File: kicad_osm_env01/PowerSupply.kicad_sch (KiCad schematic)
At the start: 28 parts, among them J5 USB_C_Receptacle_USB2.0, U1 LM66100DCKR, U4 LM66100DCKR, U9 TLV1117LV33DCYR

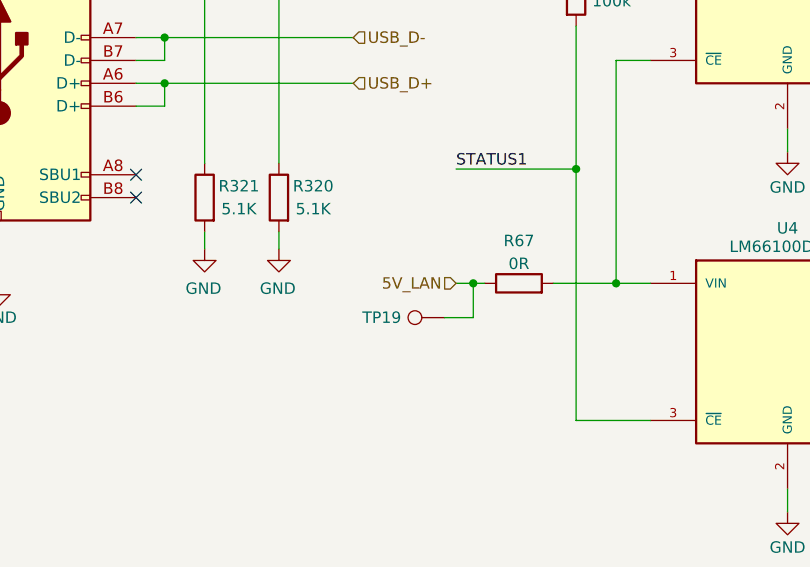
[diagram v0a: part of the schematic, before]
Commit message: locked in main connectors for connector end on layout
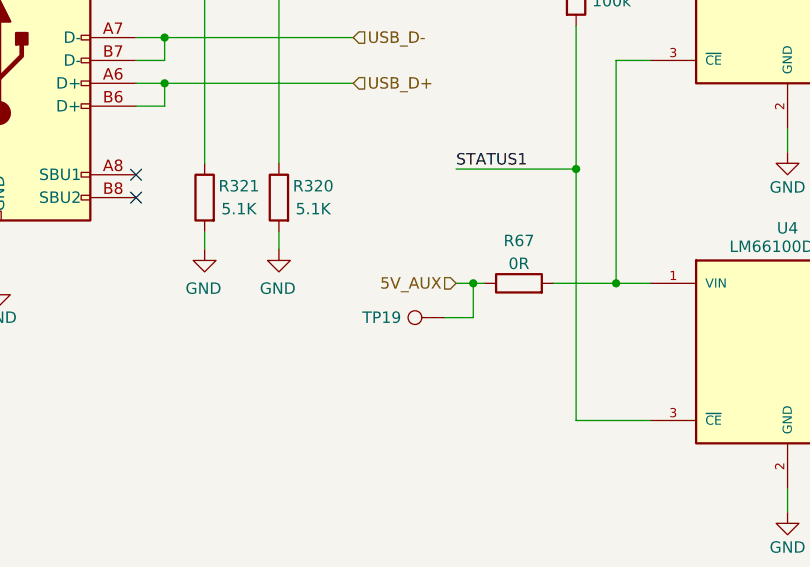
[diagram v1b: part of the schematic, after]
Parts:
- J5: footprint Footprints:MOLEX_216989-0001 -> Devtank_PCB_lib:216989-0001_MOL
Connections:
- net 5V_LAN renamed 5V_AUX
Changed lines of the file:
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@@
     (effects (font (size 1.27 1.27)) (justify left))
   )
-  (hierarchical_label "5V_LAN" (shape input) (at 81.28 75.565 180) (fields_autoplaced)
+  (hierarchical_label "5V_AUX" (shape input) (at 81.28 75.565 180) (fields_autoplaced)
     (effects (font (size 1.27 1.27)) (justify right))
   )
@@
       (effects (font (size 1.27 1.27)))
     )
-    (property "Footprint" "Footprints:MOLEX_216989-0001" (at 34.29 50.8 0)
-      (effects (font (size 1.27 1.27)) hide)
-    )
+    (property "Footprint" "Devtank_PCB_lib:216989-0001_MOL" (at 34.29 50.8 0)
+      (effects (font (size 1.27 1.27)) hide)
+    )

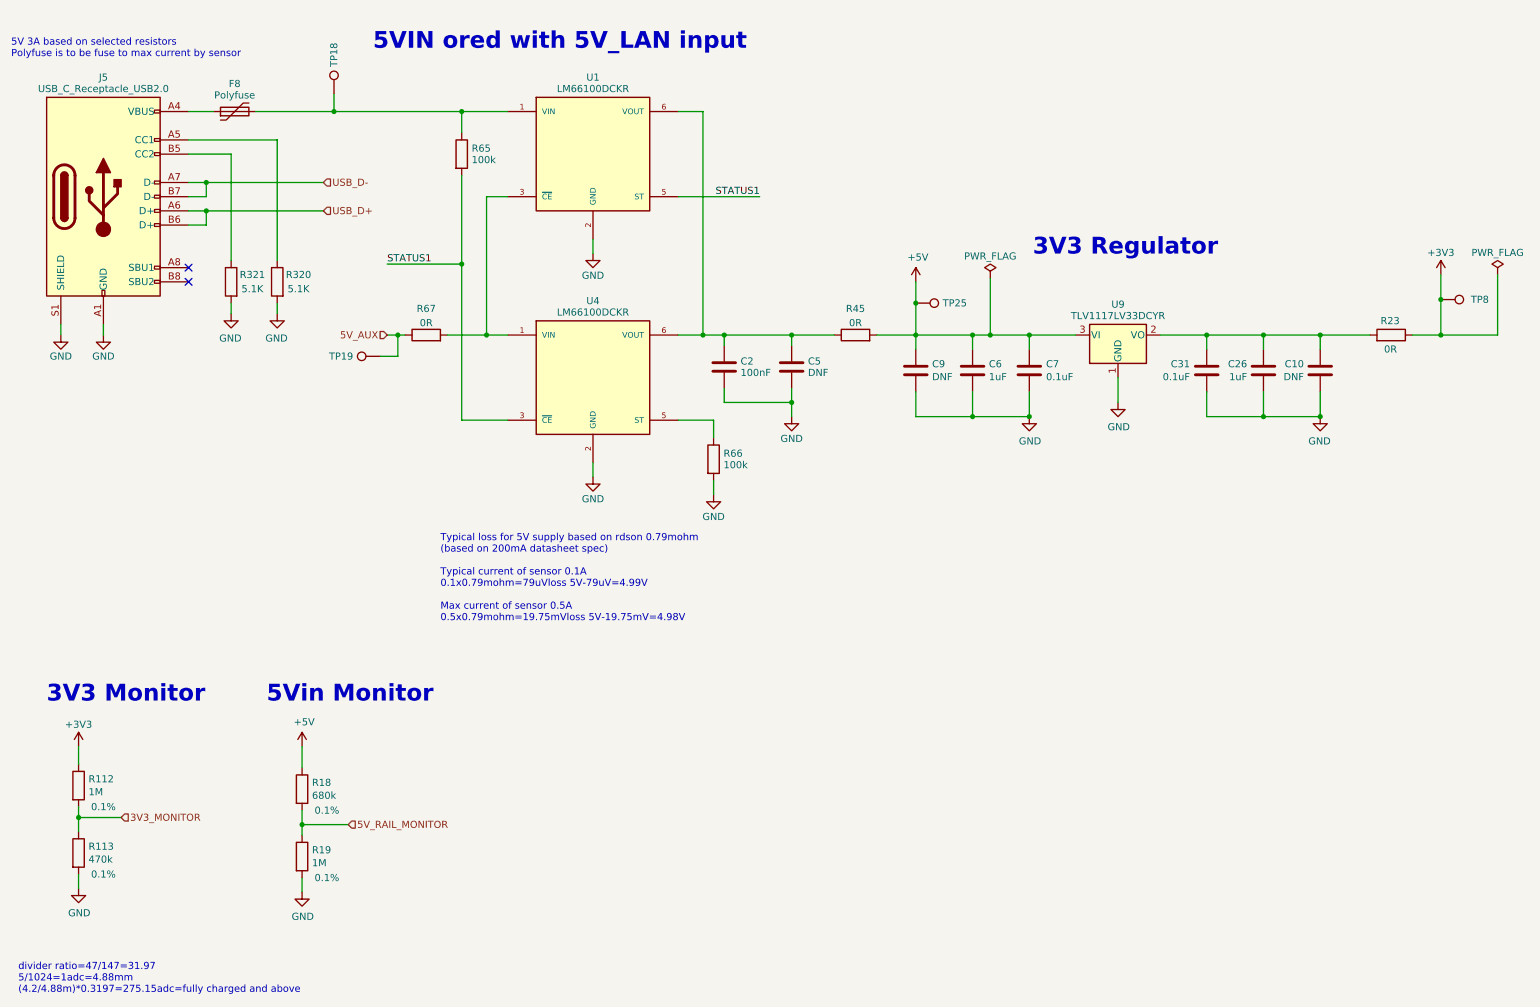
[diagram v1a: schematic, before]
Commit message: assigned all footprints
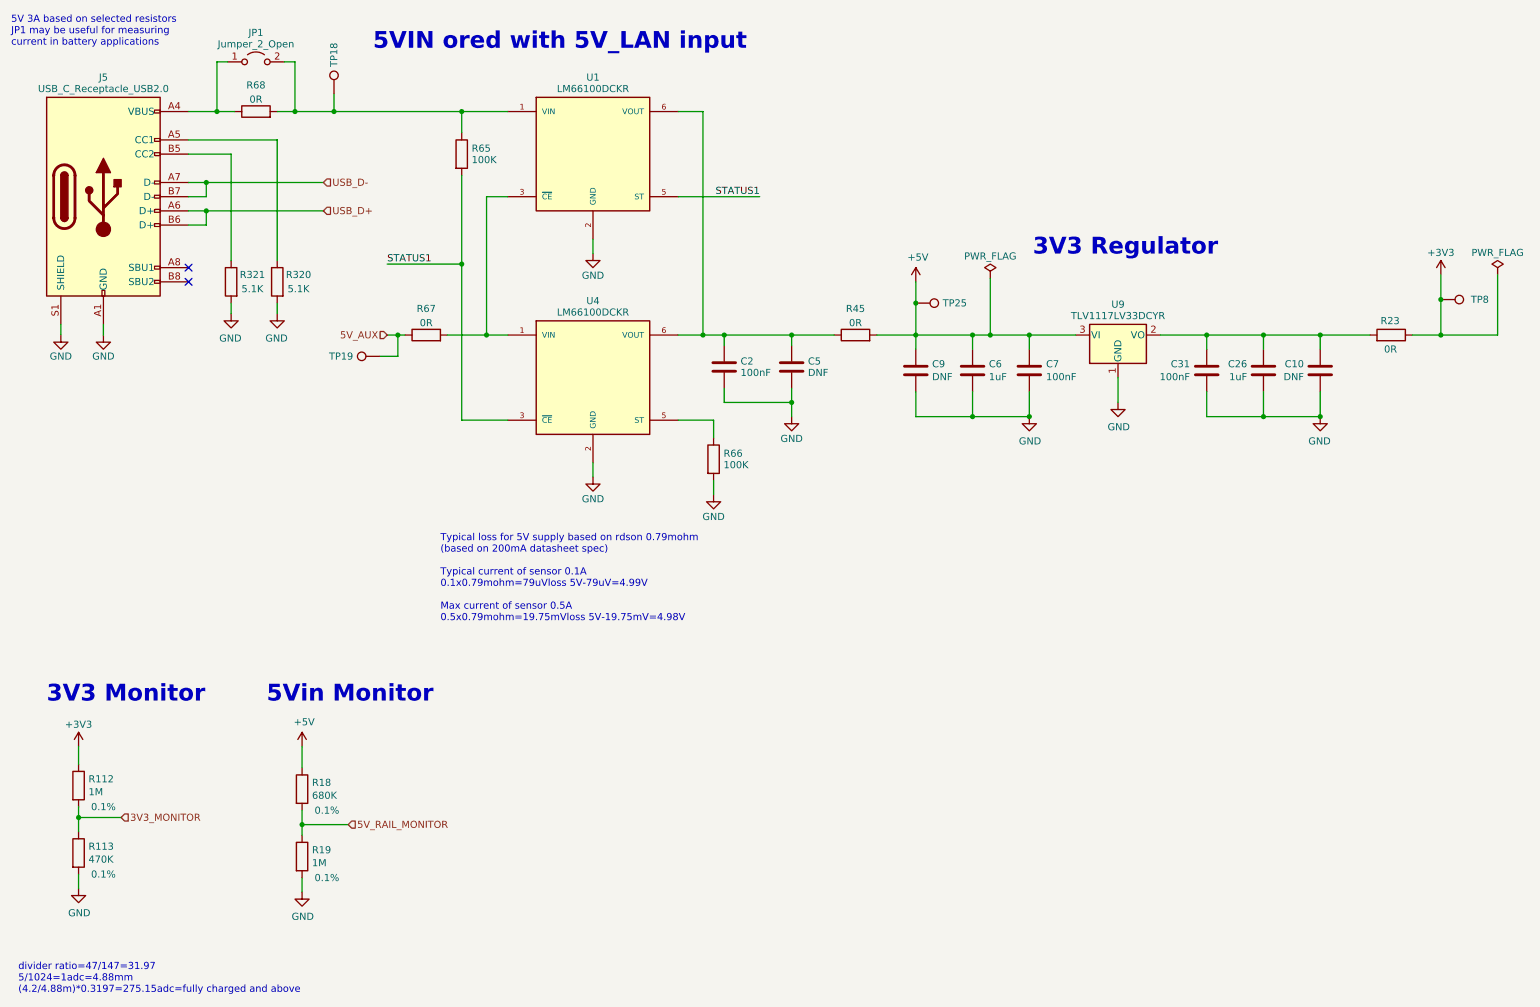
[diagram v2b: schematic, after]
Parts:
- removed F8: Polyfuse, symbol Device:Polyfuse
- added JP1: Jumper_2_Open, Connector_PinSocket_2.54mm:PinSocket_1x02_P2.54mm_Vertical, symbol Jumper:Jumper_2_Open
- added R68: 0R, Resistor_SMD:R_0805_2012Metric, symbol Device:R
- C10, C9: footprint Capacitor_SMD:C_0402_1005Metric -> Capacitor_SMD:C_1206_3216Metric
- C2: footprint (none) -> Capacitor_SMD:C_0805_2012Metric; Voltage (none) -> 50V
- C26, C6: footprint Capacitor_SMD:C_0402_1005Metric -> Capacitor_SMD:C_0805_2012Metric
- C31, C7: value 0.1uF -> 100nF; footprint Capacitor_SMD:C_0603_1608Metric -> Capacitor_SMD:C_0805_2012Metric; Voltage (none) -> 50V
- C5: footprint (none) -> Capacitor_SMD:C_0805_2012Metric
- R113: value 470k -> 470K
- R18: value 680k -> 680K
- R23, R45: footprint Resistor_SMD:R_0603_1608Metric -> Resistor_SMD:R_0805_2012Metric
- R320, R321: Tolerance 1% -> (none)
- R65, R66: value 100k -> 100K; footprint (none) -> Resistor_SMD:R_0402_1005Metric
- R67: footprint Resistor_SMD:R_0603_1608Metric -> Resistor_SMD:R_0402_1005Metric
- U1, U4: footprint (none) -> Package_TO_SOT_SMD:SOT-363_SC-70-6
- U9: footprint (none) -> Package_TO_SOT_SMD:SOT-223-3_TabPin2
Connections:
- net at R65.1, TP18.1, U1.1 (VIN): now also JP1.2 (B), R68.2
- net at J5.A4 (VBUS), J5.A9 (VBUS), J5.B4 (VBUS)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: now also JP1.1 (A), R68.1
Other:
- note added: "5V 3A based on selected resistors JP1 may be useful for measuring current in battery applications"
- note removed: "5V 3A based on selected resistors Polyfuse is to be fuse to max current by sensor"

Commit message: started layout throwdown
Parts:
- removed C2: 100nF, Capacitor_SMD:C_0805_2012Metric, symbol Device:C
- removed C5: DNF, Capacitor_SMD:C_0805_2012Metric, symbol Device:C
- R67: footprint Resistor_SMD:R_0402_1005Metric -> Resistor_SMD:R_0805_2012Metric
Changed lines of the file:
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@@
   (junction (at 186.055 90.17) (diameter 0) (color 0 0 0 0)
   )
-  (junction (at 141.605 75.565) (diameter 0) (color 0 0 0 0)
-  )
   (junction (at 248.285 75.565) (diameter 0) (color 0 0 0 0)
   )
@@
   (junction (at 186.055 75.565) (diameter 0) (color 0 0 0 0)
   )
-  (junction (at 153.67 75.565) (diameter 0) (color 0 0 0 0)
-  )
   (junction (at 48.895 48.26) (diameter 0) (color 0 0 0 0)
   )
   (junction (at 175.895 69.85) (diameter 0) (color 0 0 0 0)
-  )
-  (junction (at 153.67 87.63) (diameter 0) (color 0 0 0 0)
   )
   (junction (at 248.285 90.17) (diameter 0) (color 0 0 0 0)
@@
     (stroke (width 0) (type default))
   )
-  (wire (pts (xy 141.605 77.47) (xy 141.605 75.565))
-    (stroke (width 0) (type default))
-  )
   (wire (pts (xy 48.895 55.88) (xy 48.895 53.34))
     (stroke (width 0) (type default))
@@
     (stroke (width 0) (type default))
   )
-  (wire (pts (xy 141.605 85.09) (xy 141.605 87.63))
-    (stroke (width 0) (type default))
-  )
   (wire (pts (xy 94.615 62.865) (xy 81.28 62.865))
     (stroke (width 0) (type default))
@@
     (stroke (width 0) (type default))
   )
-  (wire (pts (xy 153.67 87.63) (xy 153.67 90.17))
-    (stroke (width 0) (type default))
-  )
   (wire (pts (xy 238.125 85.725) (xy 238.125 90.17))
     (stroke (width 0) (type default))
@@
     (stroke (width 0) (type default))
   )
-  (wire (pts (xy 141.605 75.565) (xy 137.795 75.565))
-    (stroke (width 0) (type default))
-  )
   (wire (pts (xy 204.47 75.565) (xy 196.215 75.565))
     (stroke (width 0) (type default))
@@
     (stroke (width 0) (type default))
   )
-  (wire (pts (xy 153.67 75.565) (xy 161.29 75.565))
-    (stroke (width 0) (type default))
-  )
   (wire (pts (xy 175.895 85.725) (xy 175.895 90.17))
     (stroke (width 0) (type default))
@@
     (stroke (width 0) (type default))
   )
-  (wire (pts (xy 153.67 77.47) (xy 153.67 75.565))
-    (stroke (width 0) (type default))
-  )
-  (wire (pts (xy 153.67 87.63) (xy 153.67 85.09))
-    (stroke (width 0) (type default))
-  )
   (wire (pts (xy 248.285 90.17) (xy 238.125 90.17))
     (stroke (width 0) (type default))
@@
     (stroke (width 0) (type default))
   )
-  (wire (pts (xy 141.605 87.63) (xy 153.67 87.63))
-    (stroke (width 0) (type default))
-  )
-  (wire (pts (xy 153.67 75.565) (xy 141.605 75.565))
+  (wire (pts (xy 137.795 75.565) (xy 161.29 75.565))
     (stroke (width 0) (type default))
   )
@@
     )
   )
-  (symbol (lib_id "Device:C") (at 153.67 81.28 0) (unit 1)
-    (in_bom yes) (on_board yes) (dnp no)
-    (property "Reference" "C5" (at 156.591 80.256 0)
-      (effects (font (size 1.27 1.27)) (justify left))
-    )
-    (property "Value" "DNF" (at 156.591 82.304 0)
-      (effects (font (size 1.27 1.27)) (justify left))
-    )
-    (property "Footprint" "Capacitor_SMD:C_0805_2012Metric" (at 154.6352 85.09 0)
-      (effects (font (size 1.27 1.27)) hide)
-    )
-    (property "Datasheet" "" (at 153.67 81.28 0)
-      (effects (font (size 1.27 1.27)) hide)
-    )
-    (pin "1")
-    (pin "2")
-    (instances
-      (project "OSM_env01"
-        (path "/ab8b0540-9c9f-4195-88f5-7bed0b0a8ed6"
-          (reference "C5") (unit 1)
-        )
-        (path "/ab8b0540-9c9f-4195-88f5-7bed0b0a8ed6/00000000-0000-0000-0000-000060688d25"
-          (reference "C5") (unit 1)
-        )
-      )
-    )
-  )
   (symbol (lib_id "power:GND") (at 26.035 174.625 0) (unit 1)
     (in_bom yes) (on_board yes) (dnp no)
@@
       (effects (font (size 1.27 1.27)))
     )
-    (property "Footprint" "Resistor_SMD:R_0402_1005Metric" (at 88.265 77.343 90)
+    (property "Footprint" "Resistor_SMD:R_0805_2012Metric" (at 88.265 77.343 90)
       (effects (font (size 1.27 1.27)) hide)
     )
@@
         (path "/ab8b0540-9c9f-4195-88f5-7bed0b0a8ed6/00000000-0000-0000-0000-000060688d25"
           (reference "#PWR041") (unit 1)
-        )
-      )
-    )
-  )
-  (symbol (lib_id "Device:C") (at 141.605 81.28 0) (unit 1)
-    (in_bom yes) (on_board yes) (dnp no) (fields_autoplaced)
-    (property "Reference" "C2" (at 144.526 80.256 0)
-      (effects (font (size 1.27 1.27)) (justify left))
-    )
-    (property "Value" "100nF" (at 144.526 82.304 0)
-      (effects (font (size 1.27 1.27)) (justify left))
-    )
-    (property "Footprint" "Capacitor_SMD:C_0805_2012Metric" (at 142.5702 85.09 0)
-      (effects (font (size 1.27 1.27)) hide)
-    )
-    (property "Datasheet" "" (at 141.605 81.28 0)
-      (effects (font (size 1.27 1.27)) hide)
-    )
-    (property "Voltage" "50V" (at 141.605 81.28 0)
-      (effects (font (size 1.27 1.27)) hide)
-    )
-    (pin "1")
-    (pin "2")
-    (instances
-      (project "OSM_env01"
-        (path "/ab8b0540-9c9f-4195-88f5-7bed0b0a8ed6"
-          (reference "C2") (unit 1)
-        )
-        (path "/ab8b0540-9c9f-4195-88f5-7bed0b0a8ed6/00000000-0000-0000-0000-000060688d25"
-          (reference "C2") (unit 1)
         )
       )
@@
         )
       )
-    )
-  )
-  (symbol (lib_id "OSM_env01:GND") (at 153.67 90.17 0) (unit 1)
-    (in_bom yes) (on_board yes) (dnp no) (fields_autoplaced)
-    (property "Reference" "#PWR087" (at 153.67 96.52 0)
-      (effects (font (size 1.27 1.27)) hide)
-    )
-    (property "Value" "GND" (at 153.67 94.115 0)
-      (effects (font (size 1.27 1.27)))
-    )
-    (property "Footprint" "" (at 153.67 90.17 0)
-      (effects (font (size 1.524 1.524)))
-    )
-    (property "Datasheet" "" (at 153.67 90.17 0)
-      (effects (font (size 1.524 1.524)))
-    )
-    (pin "1")
-    (instances
-      (project "OSM_env01"
-        (path "/ab8b0540-9c9f-4195-88f5-7bed0b0a8ed6"
-          (reference "#PWR087") (unit 1)
-        )
-        (path "/ab8b0540-9c9f-4195-88f5-7bed0b0a8ed6/00000000-0000-0000-0000-000060688d25"
-          (reference "#PWR092") (unit 1)
-        )
-      )
